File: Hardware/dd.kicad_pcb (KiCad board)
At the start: 2 copper layers, 40.6 x 109.2 mm, 65 parts, among them CON1 AVR-ISP-6, J1 , J2 , J3 Conn_02x05_Odd_Even, J4 , J5 Conn_01x08_Male, J6 , Q1 MMBT3904, Q2 MMBT3904, Q3 MMBT3904, Q4 MMBT3904, Q5 MMBT3904, Q6 MMBT3904, Q7 MMBT3904, Q8 MMBT3904, U1 ATMEGA328P-AU, U2 MCP23S17, U3 LM1117-5.0, U4 MCP6002-xSN, Y1 20MHz

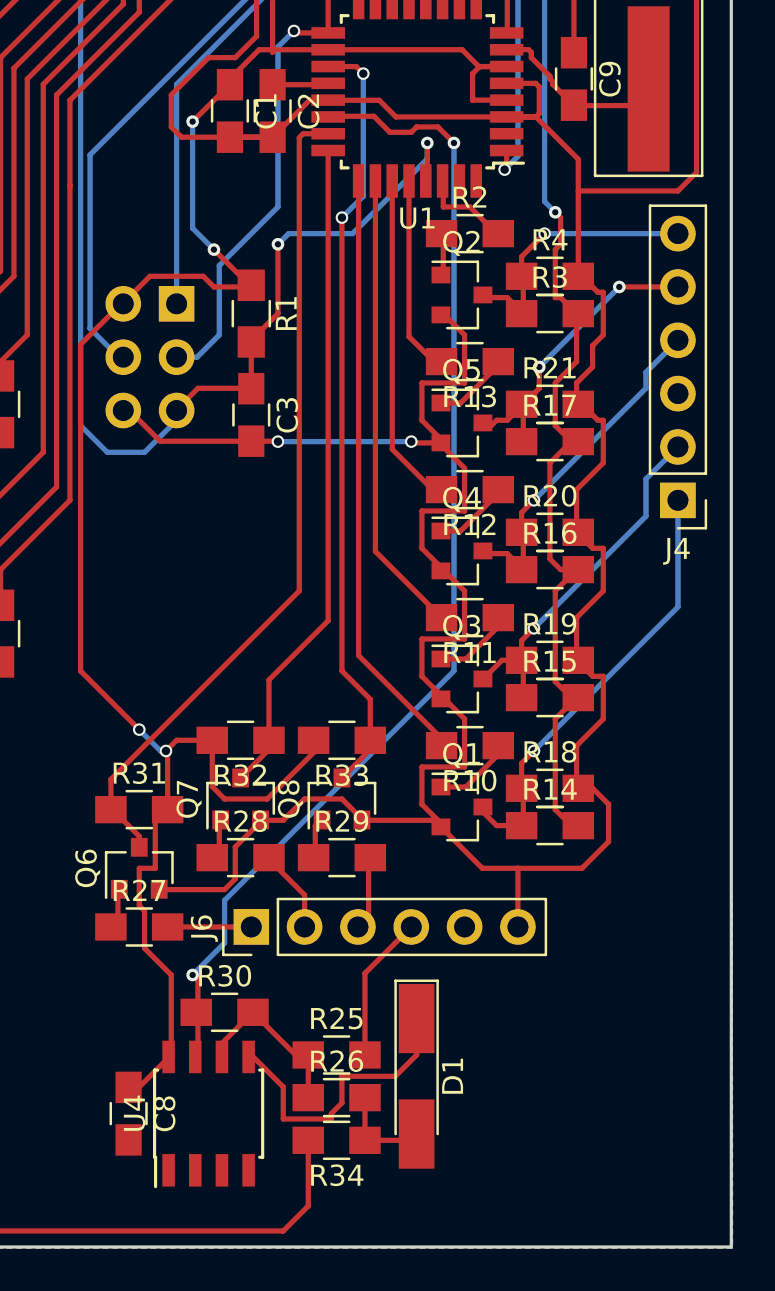
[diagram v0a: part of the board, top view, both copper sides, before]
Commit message: LED4 added
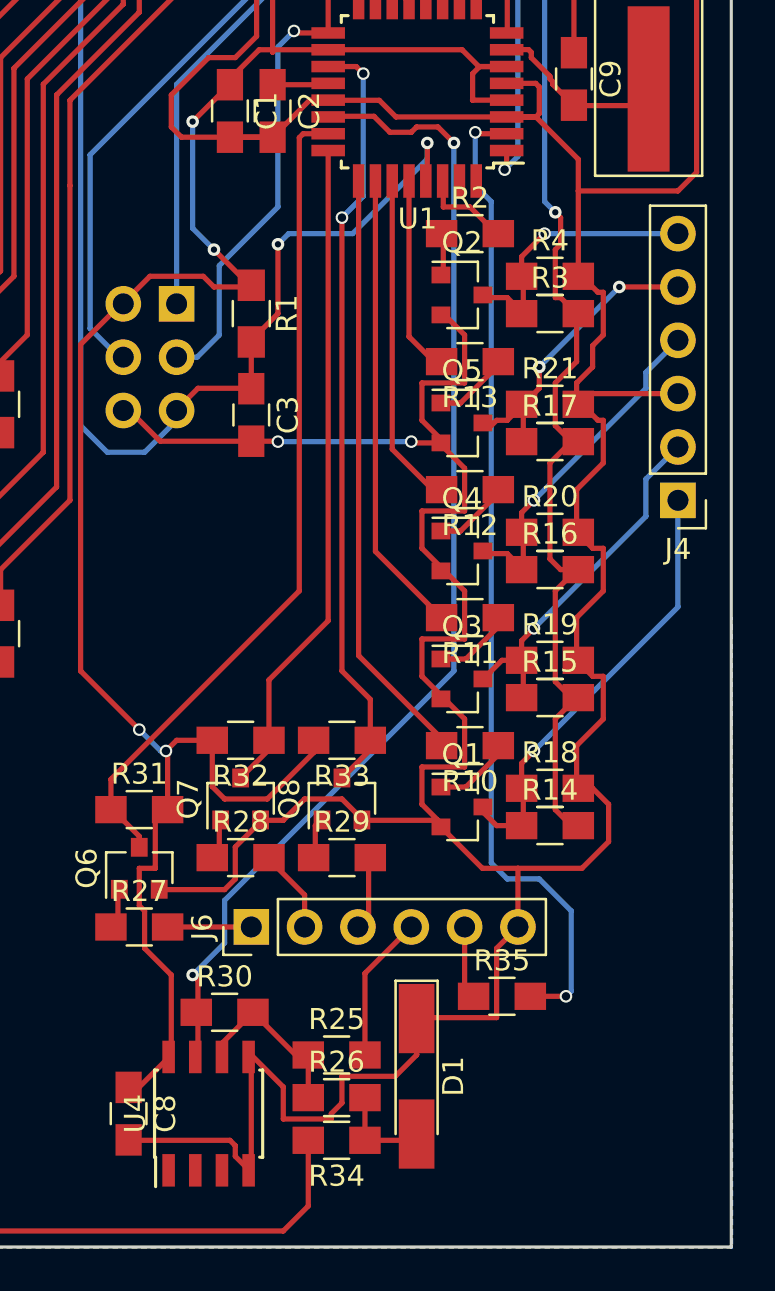
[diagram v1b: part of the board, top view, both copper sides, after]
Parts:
- added R35: 1K, Resistors_SMD:R_0805_HandSoldering, F.Cu at (80.5, 181.1)
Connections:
- J1 pad 5: (no net) -> Net-(J1-Pad5)
- J2 pad 4: (no net) -> Net-(J2-Pad4)
- J2 pad 8: (no net) -> Net-(J2-Pad8)
- J5 pad 6: (no net) -> Net-(J5-Pad6)
- J6 pad 5: (no net) -> Net-(J6-Pad5)
- U1 pad 2: (no net) -> /LED4
- U1 pad 31: (no net) -> Net-(U1-Pad31)
- U1 pad 32: (no net) -> Net-(U1-Pad32)
- U2 pad 19: (no net) -> Net-(U2-Pad19)
- U2 pad 20: (no net) -> Net-(U2-Pad20)
- U2 pad 7: (no net) -> Net-(U2-Pad7)
- U4 pad 1: (no net) -> Net-(U4-Pad1)
- U4 pad 2: (no net) -> Net-(U4-Pad2)
- U4 pad 3: (no net) -> Net-(U4-Pad3)
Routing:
- net /LED4: track 0.00 -> 47.3 mm, vias 0 -> 2
- net GND: track 328.9 -> 355.5 mm
- net Net-(J6-Pad5): track 0.00 -> 3.59 mm

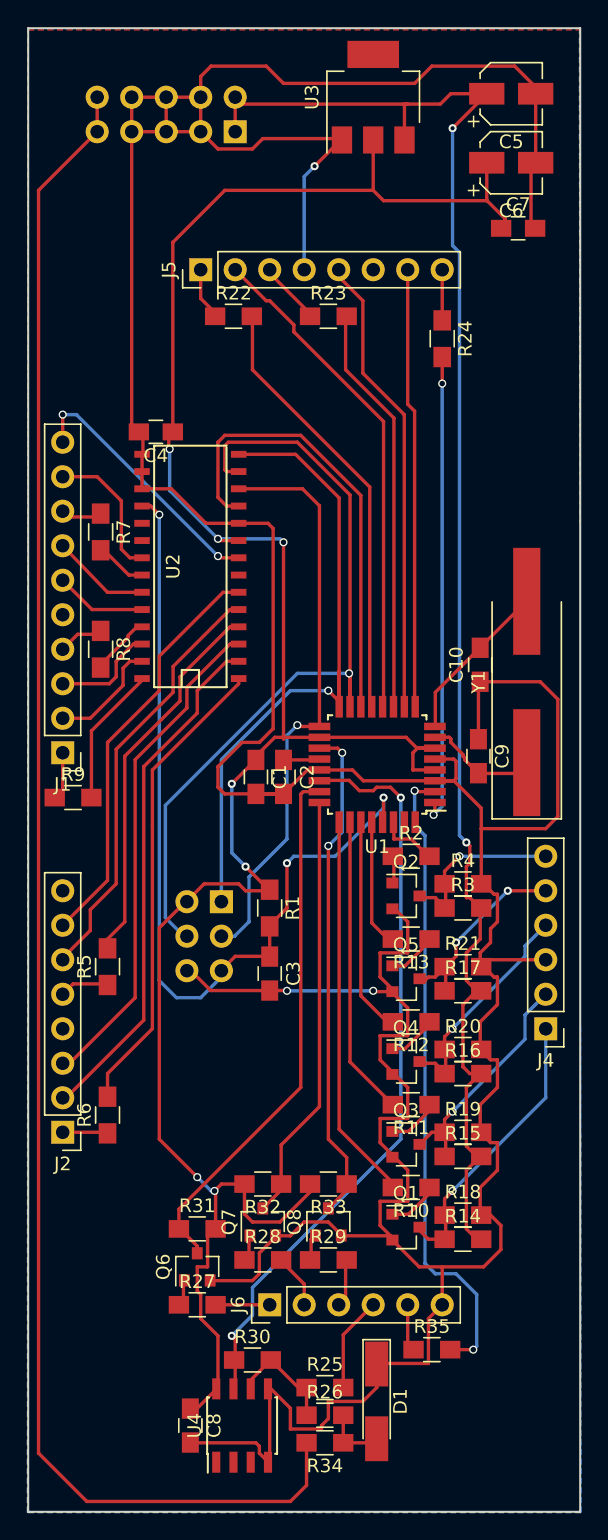
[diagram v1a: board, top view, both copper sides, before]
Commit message: change Mod from pin19 to 31, add debug
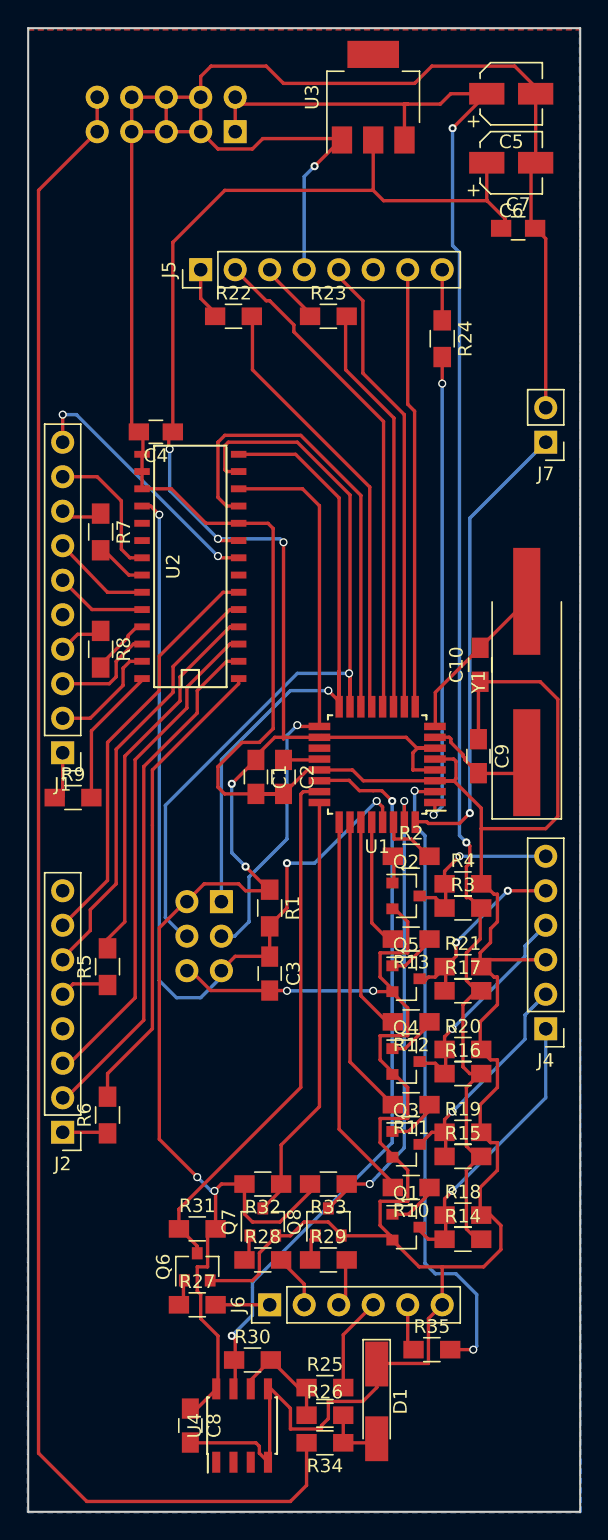
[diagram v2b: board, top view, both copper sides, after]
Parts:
- added J7: Conn_01x02_Male, Pin_Headers:Pin_Header_Straight_1x02_Pitch2.54mm, F.Cu at (88.9, 114.3)
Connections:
- U1 pad 19: /Mod -> Net-(U1-Pad19)
- U1 pad 31: Net-(U1-Pad31) -> /Mod
- U1 pad 32: Net-(U1-Pad32) -> /Debug
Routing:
- net /Debug: track 0.00 -> 34.1 mm, vias 0 -> 1
- net GND: track 355.5 -> 369.0 mm
- net /Mod: track 36.9 -> 34.8 mm
- net /CV: track 56.0 -> 54.7 mm
- net Net-(C3-Pad1): track 65.5 -> 64.4 mm
